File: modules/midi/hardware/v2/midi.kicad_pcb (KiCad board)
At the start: 2 copper layers, 19 x 110 mm, 62 parts, among them J1 PJ366ST, J10 Eurorack_2x5, J11 UPDI, J2 PJ301M-12, J3 PJ301M-12, J4 PJ301M-12, J5 PJ301M-12, J6 PJ301M-12, J7 PJ301M-12, J8 PJ301M-12, J9 PJ301M-12, Q1 MMBT3904, U1 ATtiny1616-MNR, U2 CJ431, U3 HT7550-1

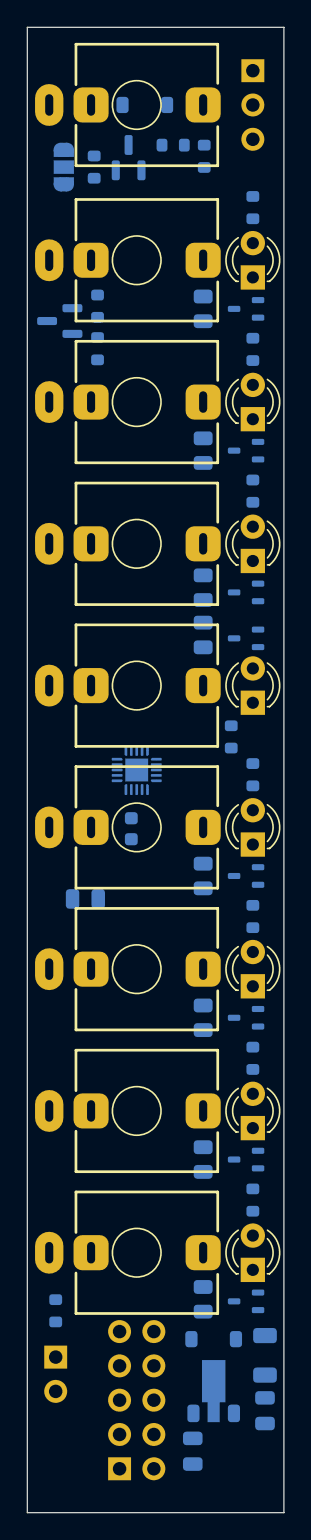
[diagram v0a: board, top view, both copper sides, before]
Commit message: midi rebuild step 4: V2 routed, exported to jlcpcb/v2, verified
Co-Authored-By: Claude Opus 5.5 <noreply@anthropic.com>
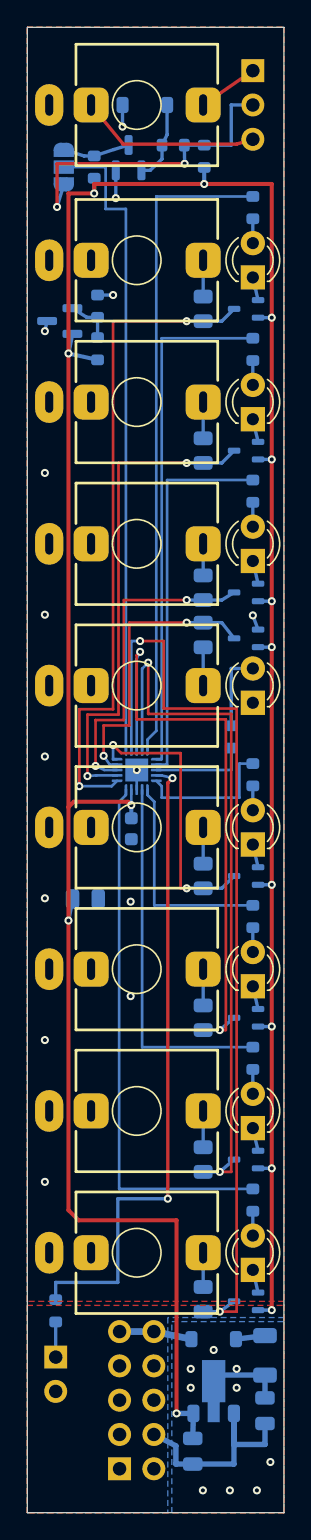
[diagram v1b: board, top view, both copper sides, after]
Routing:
- net /+5V: track 0.00 -> 223.0 mm, vias 0 -> 14
- net /CH8_TX: track 0.00 -> 69.4 mm, vias 0 -> 2
- net /CH7_TX: track 0.00 -> 54.0 mm, vias 0 -> 2
- net /CH1_TX: track 0.00 -> 49.2 mm, vias 0 -> 2
- net /CH1_LED: track 0.00 -> 48.4 mm
- net /UPDI_PA0: track 0.00 -> 48.3 mm, vias 0 -> 2
- net /RX: track 0.00 -> 47.8 mm
- net /CH6_TX: track 0.00 -> 45.2 mm, vias 0 -> 2
- net /CH8_LED: track 0.00 -> 39.7 mm
- net /CH2_LED: track 0.00 -> 38.3 mm
- net /GND: track 0.00 -> 37.6 mm, vias 0 -> 14
- net /CH2_TX: track 0.00 -> 36.6 mm, vias 0 -> 2
- net /CH3_LED: track 0.00 -> 28.2 mm
- net /CH7_LED: track 0.00 -> 27.3 mm
- net /CH3_TX: track 0.00 -> 24.4 mm, vias 0 -> 2
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- added copper zone on B.Cu, net /GND
- added copper zone on F.Cu, net /GND
- added copper zone on B.Cu, net /VIN_LDO
- added copper zone on F.Cu, net /VIN_LDO
